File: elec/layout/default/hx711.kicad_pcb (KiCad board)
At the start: 2 copper layers, 225.7 x 100.8 mm, 0 parts

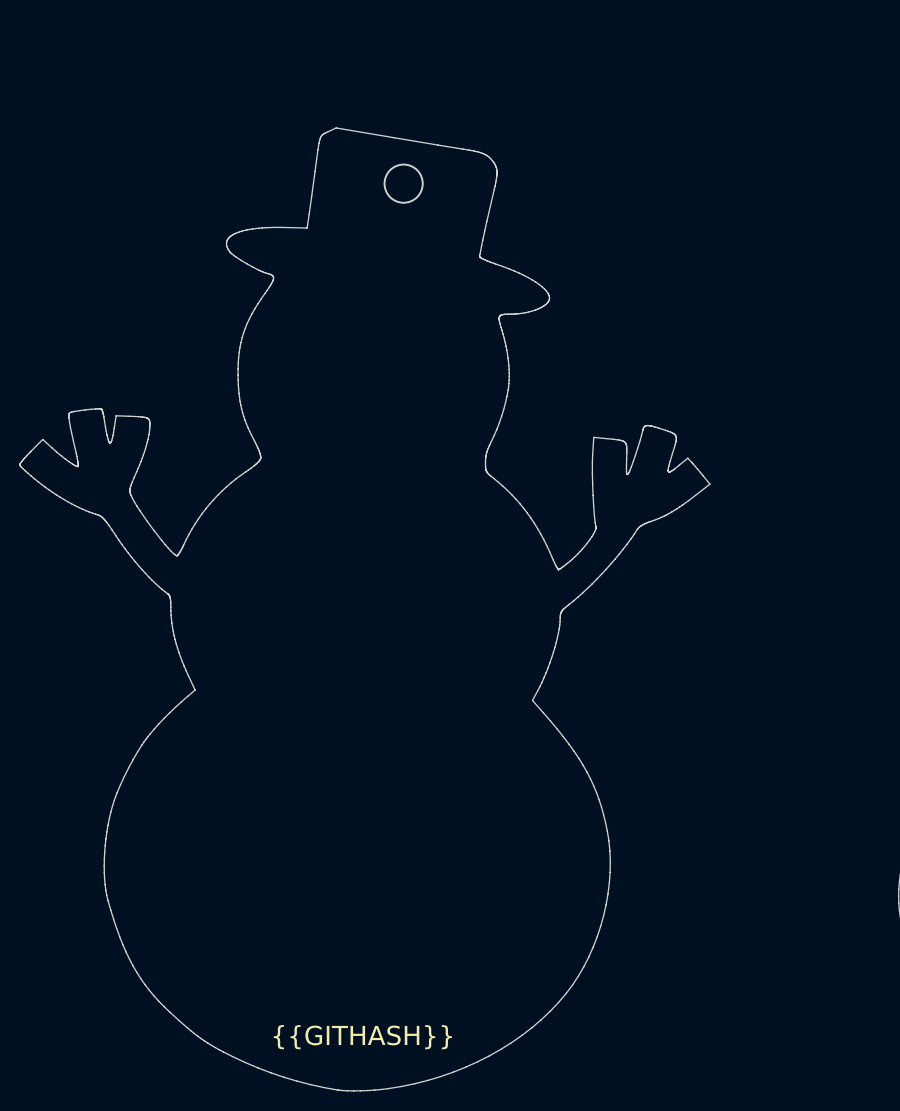
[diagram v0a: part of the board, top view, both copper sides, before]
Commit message: connect force gnd to power gnd
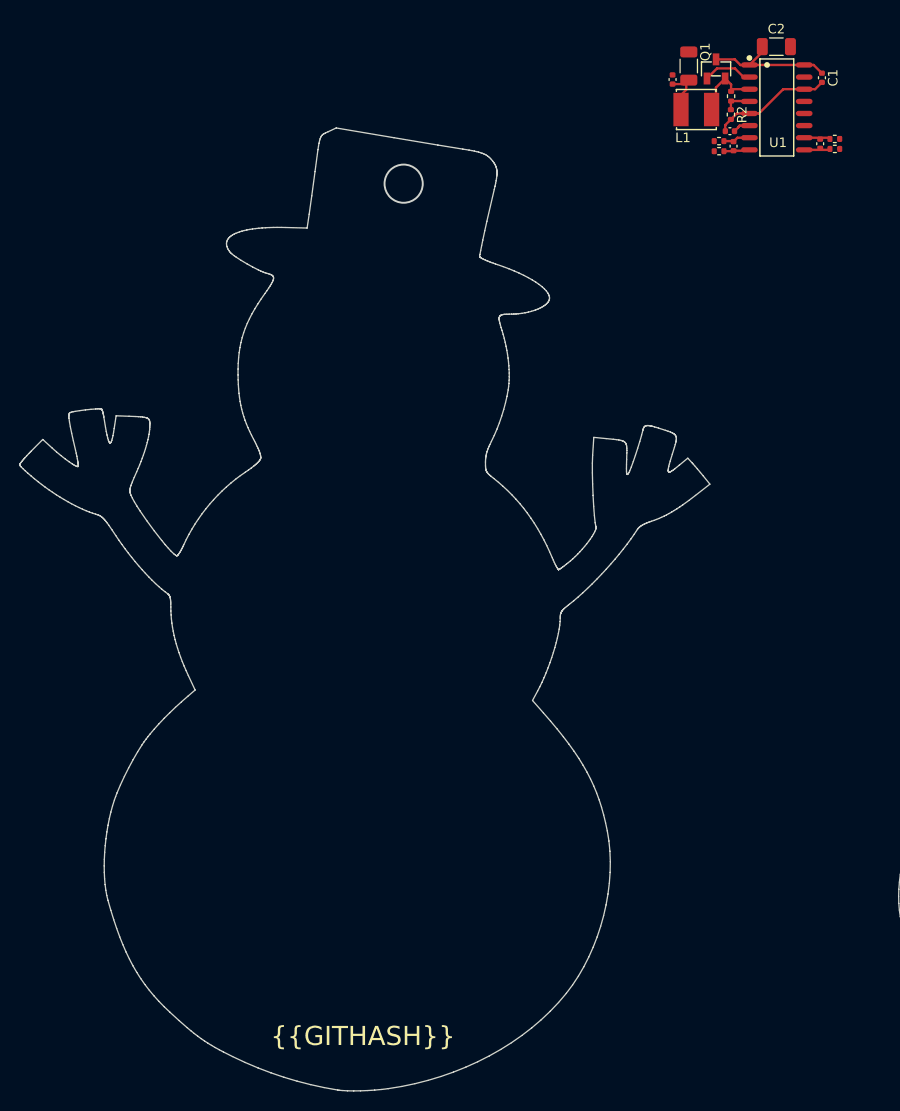
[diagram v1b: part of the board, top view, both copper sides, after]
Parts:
- added C1: Multilayer Ceramic Capacitors MLCC - SMD/SMT 100nF 10V 0402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, lib:C0402, F.Cu at (120.0, 44.5)
- added C2: Multilayer Ceramic Capacitors MLCC - SMD/SMT 10uF 16V 1206 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, lib:C1206, F.Cu at (115.2, 41.3)
- added C3: Multilayer Ceramic Capacitors MLCC - SMD/SMT 10uF 16V 1206 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, lib:C1206, F.Cu at (106.0, 43.3)
- added C4: Multilayer Ceramic Capacitors MLCC - SMD/SMT 100nF 10V 0402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, lib:C0402, F.Cu at (104.3, 44.7)
- added C5: Multilayer Ceramic Capacitors MLCC - SMD/SMT 100nF 10V 0402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, lib:C0402, F.Cu at (110.7, 51.7)
- added C6: Multilayer Ceramic Capacitors MLCC - SMD/SMT 100nF 10V 0402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, lib:C0402, F.Cu at (119.8, 51.4)
- added C7: Multilayer Ceramic Capacitors MLCC - SMD/SMT 100nF 10V 0402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, lib:C0402, F.Cu at (110.3, 50.1)
- added L1: 1.23A 3.3uH ±20% SMD Power Inductors ROHS, lib:ato-04ea3db2-4b2f-45a6-9113-aa1f8beaa754, F.Cu at (106.8, 47.8)
- added Q1: , lib:SOT-23-3_L2.9-W1.3-P1.90-LS2.4-BR, F.Cu at (108.9, 43.6)
- added R1: Chip Resistor - Surface Mount 20KOhms ±5% 1/16W 0402 RoHS, lib:R0402, F.Cu at (110.5, 46.4)
- added R2: Chip Resistor - Surface Mount 8.2KOhms ±5% 1/16W 0402 RoHS, lib:R0402, F.Cu at (110.4, 48.4)
- added R3: Chip Resistor - Surface Mount 100Ohms ±5% 1/16W 0402 RoHS, lib:R0402, F.Cu at (109.2, 52.2)
- added R4: Chip Resistor - Surface Mount 100Ohms ±5% 1/16W 0402 RoHS, lib:R0402, F.Cu at (109.2, 51.2)
- added R5: Chip Resistor - Surface Mount 100Ohms ±5% 1/16W 0402 RoHS, lib:R0402, F.Cu at (121.3, 50.9)
- added R6: Chip Resistor - Surface Mount 100Ohms ±5% 1/16W 0402 RoHS, lib:R0402, F.Cu at (121.3, 52.0)
- added U1: , lib:SOP-16_L10.0-W3.9-P1.27-LS6.0-BL, F.Cu at (115.2, 47.6)
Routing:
- net vcc: track 0.00 -> 14.2 mm
- net gnd: track 0.00 -> 12.6 mm
- net avdd: track 0.00 -> 7.45 mm
- net vcc-1: track 0.00 -> 5.29 mm
- net base: track 0.00 -> 5.25 mm
- net inna: track 0.00 -> 2.85 mm
- net vfb: track 0.00 -> 2.85 mm
- net inpb: track 0.00 -> 2.75 mm
- net innb: track 0.00 -> 2.74 mm
- net inpa: track 0.00 -> 2.72 mm
- net vbg: track 0.00 -> 1.83 mm
